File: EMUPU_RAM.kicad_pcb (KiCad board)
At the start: 2 copper layers, 99.1 x 82.5 mm, 27 parts, among them J1 Conn_01x20_Socket, J2 Conn_01x20_Socket, J3 Barrel_Jack_Switch, J4 Conn_01x06_Pin, J5 Conn_01x08_Pin, J6 Conn_01x06_Pin, J7 Conn_01x02_Pin, SW1 SW_SPDT, SW2 SW_SPST, U1 PIC18F57Q43-IPT, U2 HM678127_SOJ32_Arranged

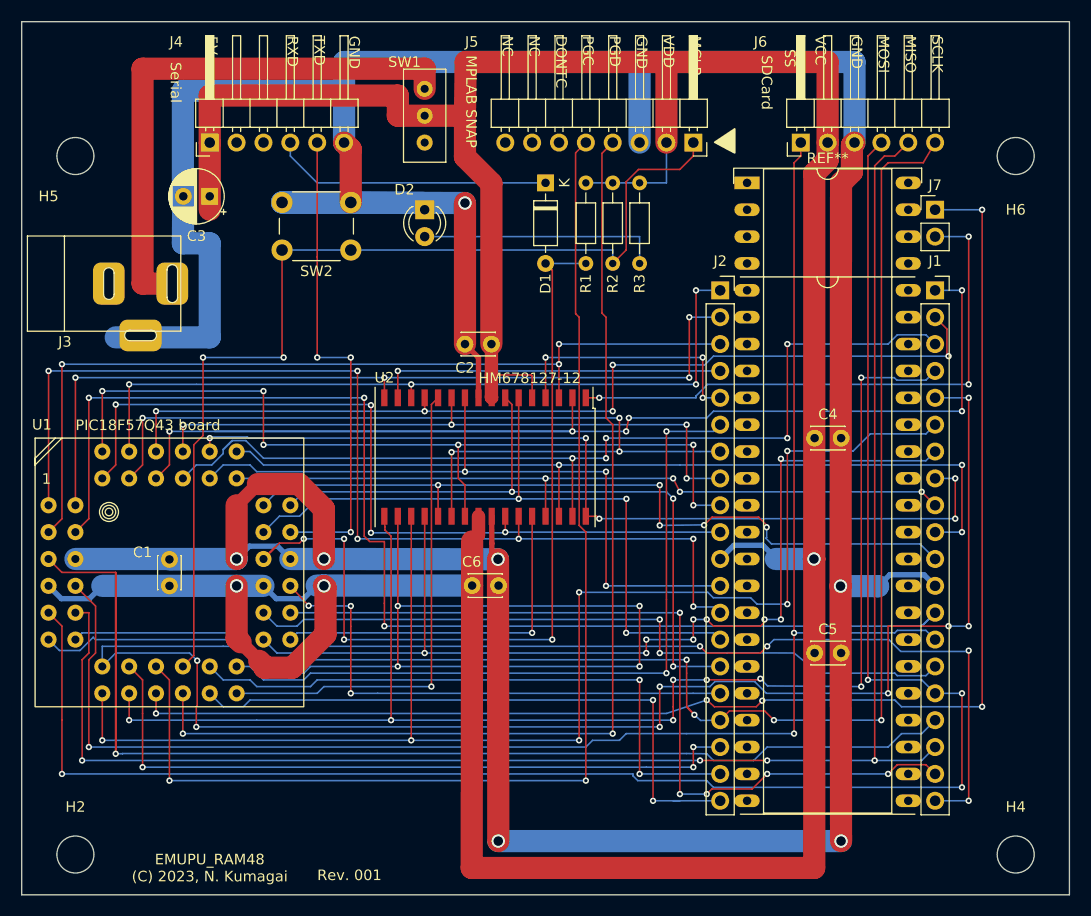
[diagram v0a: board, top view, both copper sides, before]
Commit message: Adjusting rule, described in Kosakas book, need some refinements
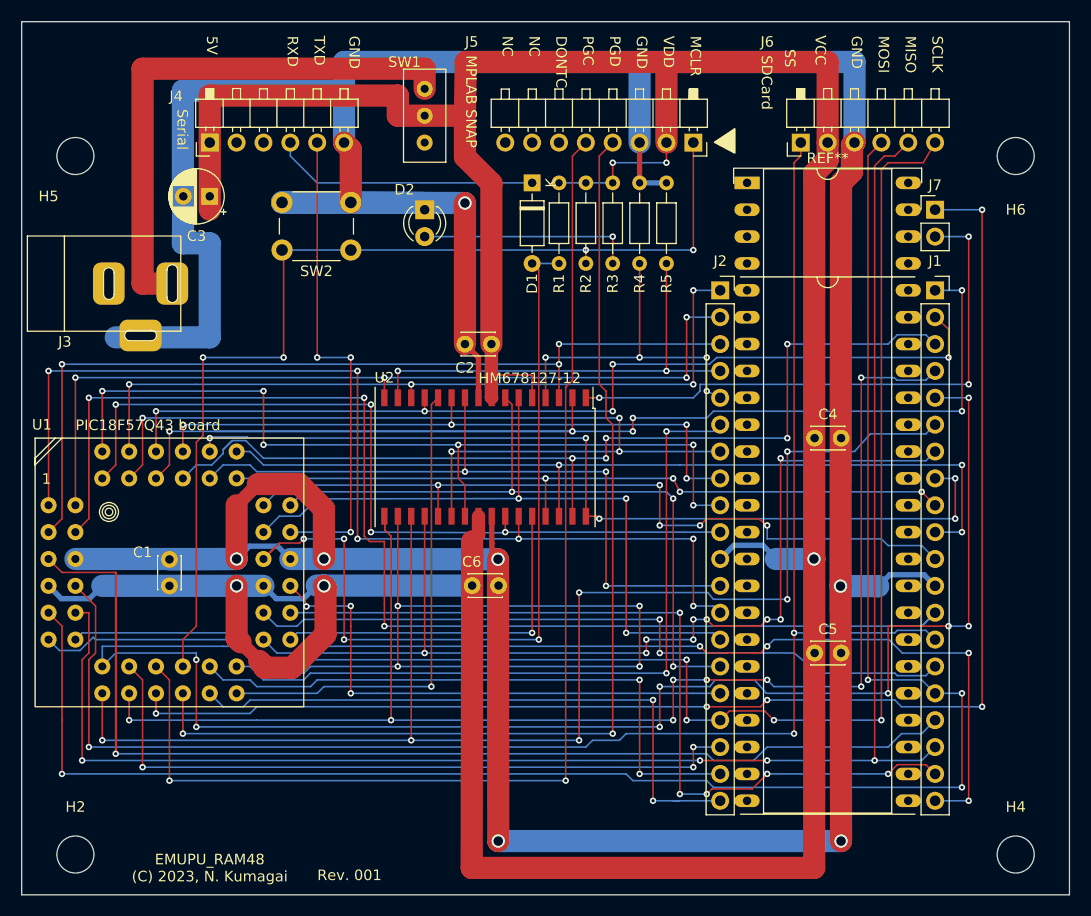
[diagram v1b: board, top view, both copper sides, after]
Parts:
- added R4: 10k, Resistor_THT:R_Axial_DIN0204_L3.6mm_D1.6mm_P7.62mm_Horizontal, F.Cu at (142.2, 81.3)
- added R5: 10k, Resistor_THT:R_Axial_DIN0204_L3.6mm_D1.6mm_P7.62mm_Horizontal, F.Cu at (144.8, 81.3)
- J4, J6: footprint Connector_PinHeader_2.54mm:PinHeader_1x06_P2.54mm_Horizontal -> 0-local:PinHeader_1x06_P2.54mm_Horizontal_NoFeet
- J5: footprint 0-local:PinHeader_1x08_P2.54mm_Rev_Horizontal -> 0-local:PinHeader_1x08_P2.54mm_Rev_Horizontal_Nofoot
- moved R3 2.54 mm to (139.7, 73.7)
- moved R1 2.54 mm to (134.6, 73.7)
- moved R2 2.54 mm to (137.2, 73.7)
- moved D1 1.27 mm to (132.1, 73.7)
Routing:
- net /A14: track 33.0 -> 43.2 mm, vias 1 -> 2
- net /A15: track 24.7 -> 32.5 mm, vias 3 -> 4
- net GND: track 391.4 -> 397.8 mm
- net Net-(D1-A): track 79.5 -> 76.9 mm
- net Net-(D2-A): track 22.9 -> 20.3 mm, vias 0 -> 1
- net VCC: track 344.1 -> 346.6 mm, vias 3 -> 5
- net Net-(J5-Pin_5): track 111.8 -> 109.9 mm
- net Net-(D1-K): track 26.5 -> 25.2 mm
- net Net-(J5-Pin_1): track 97.3 -> 98.2 mm, vias 2 -> 4
- net /A5: track 134.3 -> 133.7 mm
- net /A6: track 221.5 -> 222.0 mm

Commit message: Add Beta-filling, archive ZIP file
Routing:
- added copper zone on B.Cu, net GND
- added copper zone on F.Cu, net VCC
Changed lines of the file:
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@@
   (segment (start 105.41 123.825) (end 96.52 123.825) (width 0.1524) (layer "B.Cu") (net 59))
   (segment (start 174.625 123.19) (end 167.005 123.19) (width 0.1524) (layer "B.Cu") (net 59))
+  (zone (net 1) (net_name "VCC") (layer "F.Cu") (hatch edge 0.5)
+    (connect_pads (clearance 0.35))
+    (min_thickness 0.25) (filled_areas_thickness no)
+    (fill yes (thermal_gap 0.5) (thermal_bridge_width 0.5))
+    (polygon
+      (pts
+        (xy 84.328 58.928)
+        (xy 84.328 140.208)
+        (xy 182.372 140.208)
+        (xy 182.372 58.928)
+      )
+    )
+  )
+  (zone (net 11) (net_name "GND") (layer "B.Cu") (hatch edge 0.5)
+    (priority 1)
+    (connect_pads (clearance 0.35))
+    (min_thickness 0.25) (filled_areas_thickness no)
+    (fill yes (thermal_gap 0.5) (thermal_bridge_width 0.5))
+    (polygon
+      (pts
+        (xy 84.328 58.928)
+        (xy 84.328 140.208)
+        (xy 182.372 140.208)
+        (xy 182.372 58.928)
+      )
+    )
+  )
 )
